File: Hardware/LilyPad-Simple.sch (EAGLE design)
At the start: 43 parts, among them U1 ATMEGA328P_TQFP, U2 MCP73831, U3 MIC5219 3.3V, Y1 8MHZ

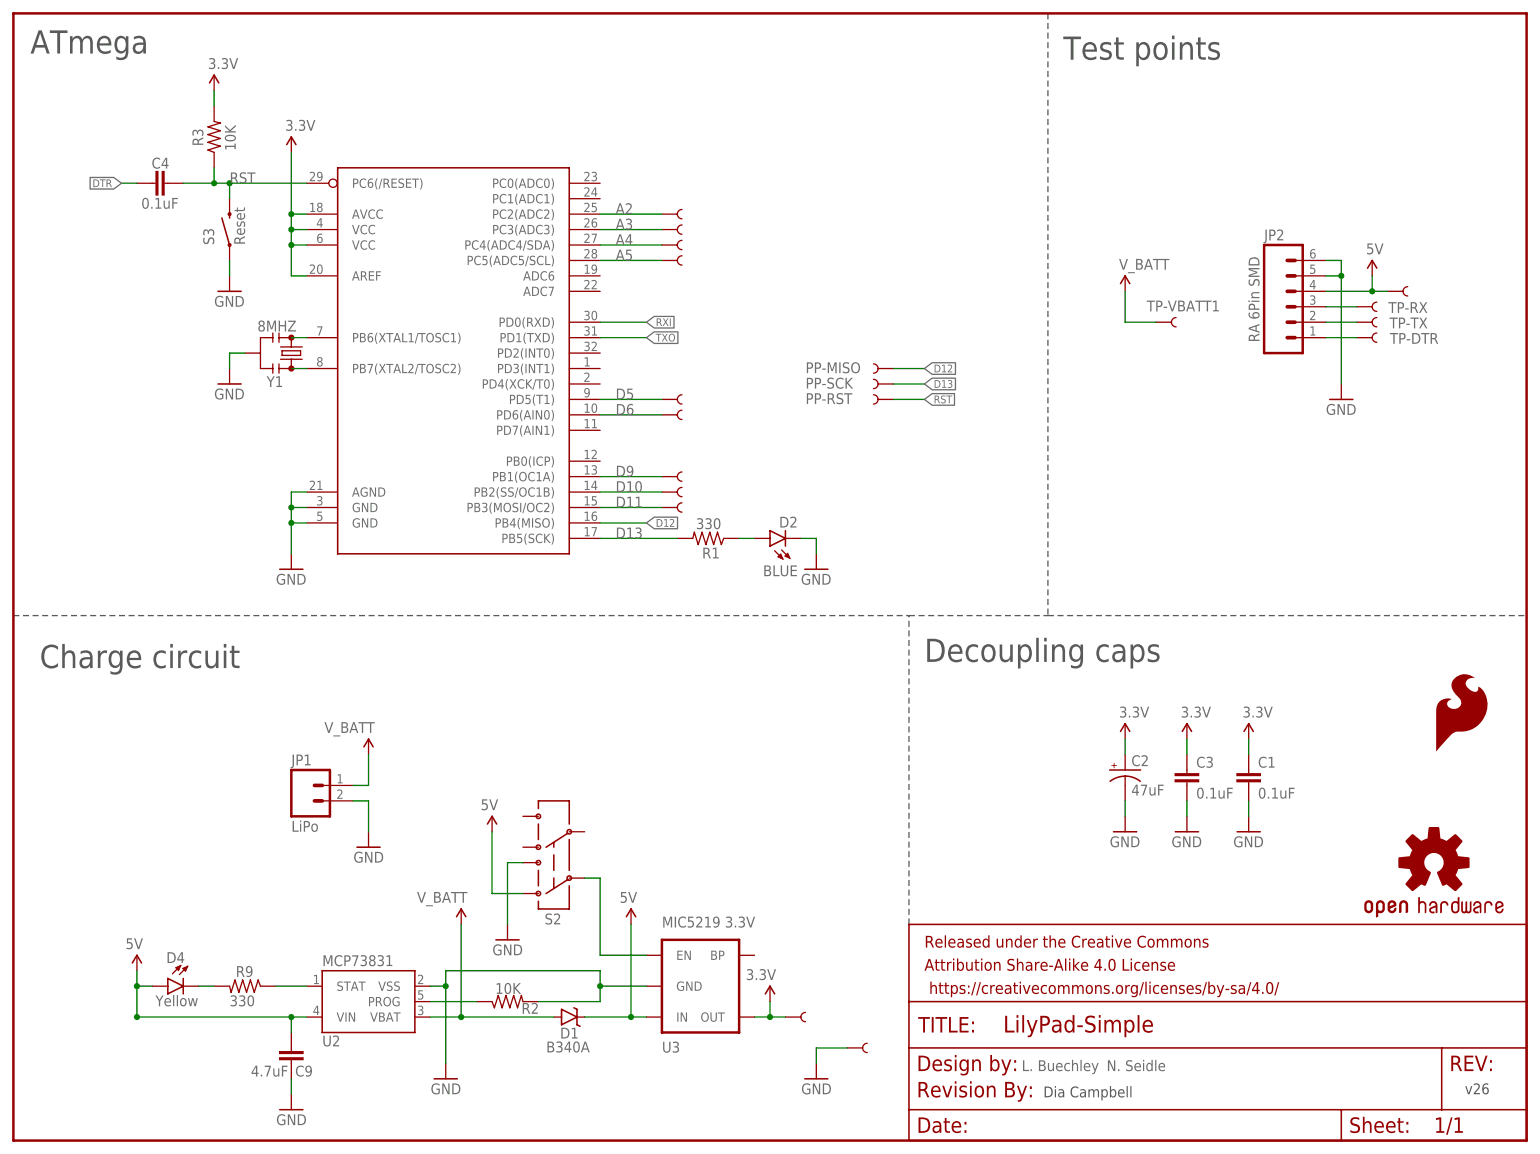
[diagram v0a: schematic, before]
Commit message: DRC changes, fixed some errors
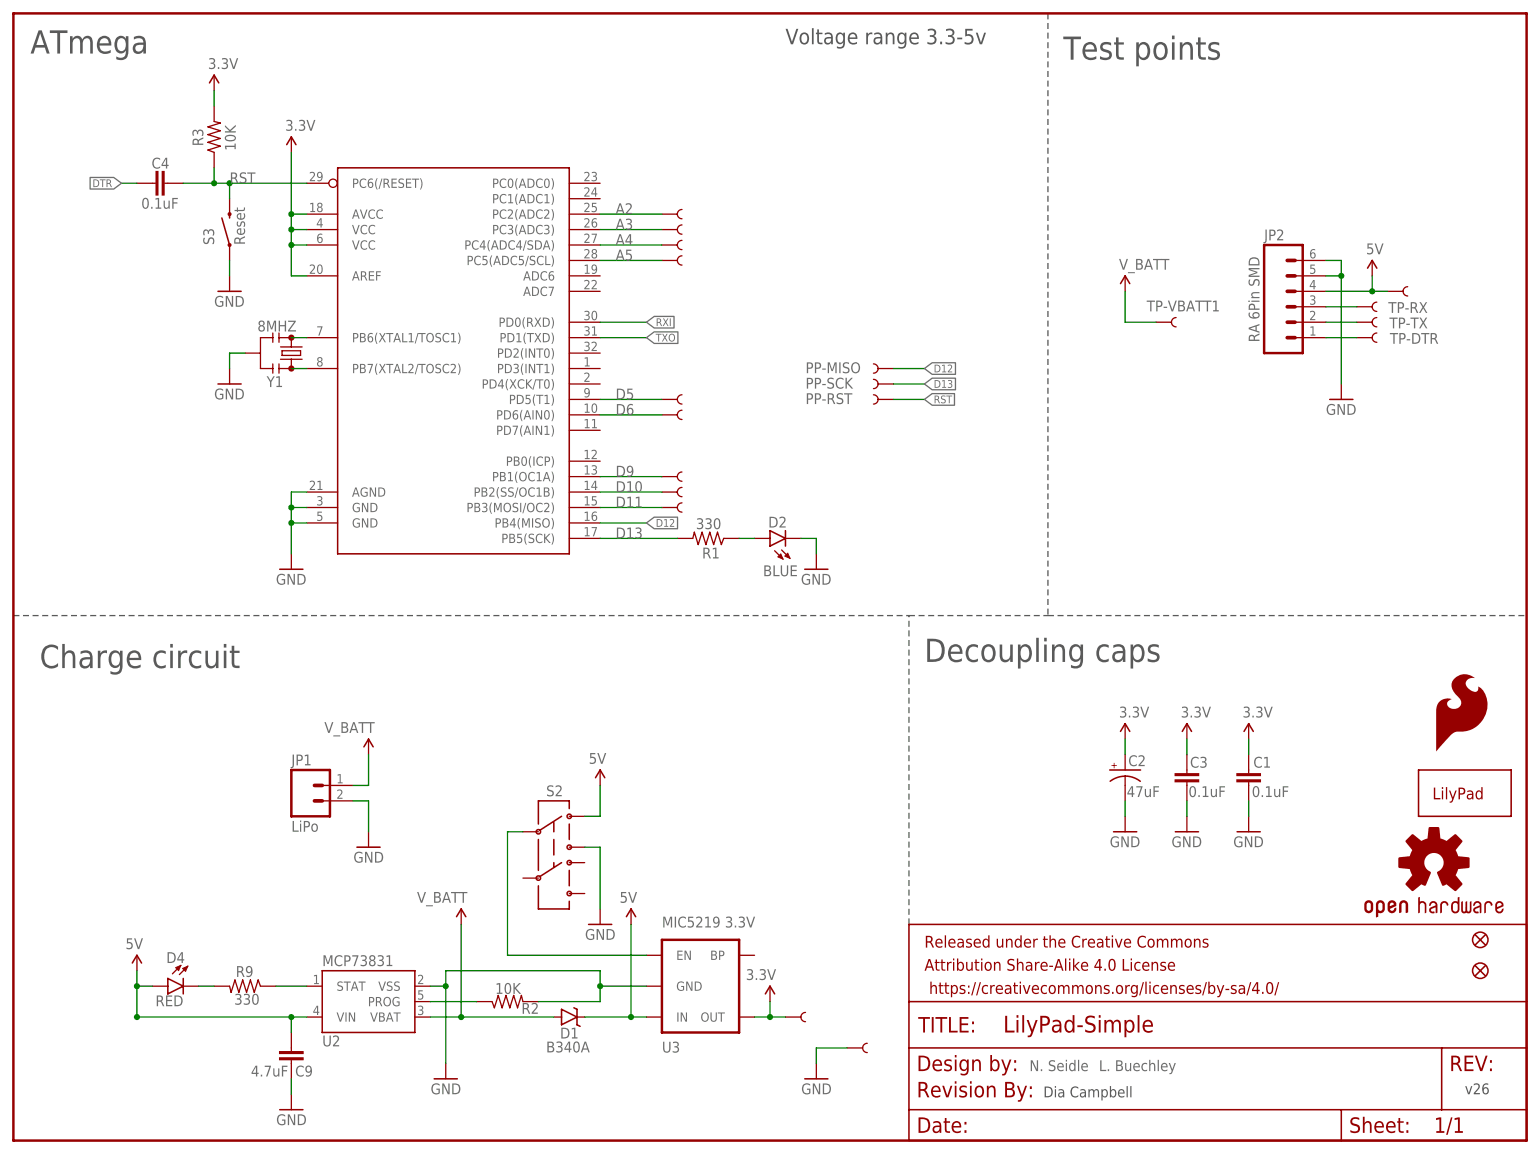
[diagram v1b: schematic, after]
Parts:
- added FID1, FID2: FIDUCIAL1X2, SparkFun-Aesthetics:FIDUCIAL1X2
- added U$2: LOGO-LPLPA, LilyPad-Wearables:LOGO-LPLPA
- D4: value Yellow -> RED; device SparkFun-LED:LED-YELLOW0603 -> SparkFun-LED:LED-RED0603
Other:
- note added: "Voltage range 3.3-5v"
- moved on the sheet: S2
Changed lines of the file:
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@@
 <part name="C9" library="SparkFun-Capacitors" deviceset="4.7UF-6.3V-10%(0603)" device="0603" value="4.7uF"/>
 <part name="GND18" library="supply1" deviceset="GND" device=""/>
-<part name="D4" library="SparkFun-LED" deviceset="LED-YELLOW" device="0603" value="Yellow"/>
+<part name="D4" library="SparkFun-LED" deviceset="LED-RED" device="0603" value="RED"/>
 <part name="R9" library="SparkFun-Resistors" deviceset="330OHM1/10W1%(0603)" device="" value="330"/>
 <part name="U2" library="SparkFun-PowerIC" deviceset="MCP73831" device=""/>
@@
 <part name="TP-VBATT1" library="SparkFun" deviceset="TEST-POINT" device="3X5" value=""/>
 <part name="SUPPLY8" library="SparkFun-Aesthetics" deviceset="V_BATT" device=""/>
+<part name="U$2" library="LilyPad-Wearables" deviceset="LOGO-LP" device="LPA"/>
+<part name="FID1" library="SparkFun-Aesthetics" deviceset="FIDUCIAL" device="1X2"/>
+<part name="FID2" library="SparkFun-Aesthetics" deviceset="FIDUCIAL" device="1X2"/>
 </parts>
 <sheets>
 <sheet>
 <plain>
-<text x="165.862" y="11.43" size="1.778" layer="95">L. Buechley</text>
-<text x="179.832" y="11.43" size="1.778" layer="95">N. Seidle</text>
+<text x="178.562" y="11.43" size="1.778" layer="95">L. Buechley</text>
+<text x="167.132" y="11.43" size="1.778" layer="95">N. Seidle</text>
 <text x="169.418" y="7.112" size="1.778" layer="97">Dia Campbell</text>
 <text x="238.76" y="7.62" size="1.778" layer="97">v26</text>
@@
 <text x="172.72" y="177.8" size="3.81" layer="97">Test points</text>
 <text x="2.794" y="178.816" size="3.81" layer="97">ATmega</text>
+<text x="127" y="180.34" size="2.54" layer="97">Voltage range 3.3-5v</text>
 </plain>
 <instances>
@@
 <instance part="A4/18" gate="G$1" x="109.22" y="147.32" smashed="yes"/>
 <instance part="D2" gate="G$1" x="124.46" y="99.06" smashed="yes" rot="R90">
-<attribute name="NAME" x="129.032" y="102.616" size="1.778" layer="95" rot="R180"/>
+<attribute name="NAME" x="127.254" y="102.616" size="1.778" layer="95" rot="R180"/>
 <attribute name="VALUE" x="129.032" y="94.615" size="1.778" layer="96" rot="R180"/>
 </instance>
@@
 <attribute name="VALUE" x="44.704" y="166.116" size="1.778" layer="96"/>
 </instance>
-<instance part="C1" gate="G$1" x="203.2" y="58.42"/>
+<instance part="C1" gate="G$1" x="203.2" y="58.42" smashed="yes">
+<attribute name="NAME" x="203.962" y="61.341" size="1.778" layer="95"/>
+<attribute name="VALUE" x="203.708" y="56.515" size="1.778" layer="96"/>
+</instance>
 <instance part="GND7" gate="1" x="203.2" y="50.8"/>
 <instance part="A5/19" gate="G$1" x="109.22" y="144.78" smashed="yes"/>
 <instance part="GND8" gate="1" x="132.08" y="10.16" rot="MR0"/>
 <instance part="U$4" gate="G$1" x="109.22" y="104.14" smashed="yes"/>
-<instance part="C2" gate="G$1" x="182.88" y="60.96"/>
-<instance part="C3" gate="G$1" x="193.04" y="58.42"/>
+<instance part="C2" gate="G$1" x="182.88" y="60.96" smashed="yes">
+<attribute name="NAME" x="183.388" y="61.595" size="1.778" layer="95"/>
+<attribute name="VALUE" x="183.134" y="56.515" size="1.778" layer="96"/>
+</instance>
+<instance part="C3" gate="G$1" x="193.04" y="58.42" smashed="yes">
+<attribute name="NAME" x="193.548" y="61.341" size="1.778" layer="95"/>
+<attribute name="VALUE" x="193.294" y="56.515" size="1.778" layer="96"/>
+</instance>
 <instance part="P+4" gate="G$1" x="203.2" y="66.04" smashed="yes">
 <attribute name="VALUE" x="202.184" y="69.596" size="1.778" layer="96"/>
@@
 </instance>
 <instance part="JP1" gate="G$1" x="48.26" y="55.88"/>
-<instance part="S2" gate="G$1" x="88.9" y="45.72" smashed="yes" rot="R180">
-<attribute name="NAME" x="87.376" y="37.338" size="1.778" layer="95" rot="MR180"/>
+<instance part="S2" gate="G$1" x="88.9" y="48.26" smashed="yes">
+<attribute name="NAME" x="90.424" y="56.642" size="1.778" layer="95" rot="MR0"/>
 </instance>
 <instance part="TP-TX" gate="G$1" x="220.98" y="134.62" smashed="yes">
@@
 <instance part="R9" gate="G$1" x="38.1" y="25.4" smashed="yes" rot="MR0">
 <attribute name="NAME" x="36.576" y="28.702" size="1.778" layer="95" rot="MR180"/>
-<attribute name="VALUE" x="35.56" y="23.876" size="1.778" layer="96" rot="MR180"/>
+<attribute name="VALUE" x="36.322" y="24.13" size="1.778" layer="96" rot="MR180"/>
 </instance>
 <instance part="U2" gate="G$1" x="58.42" y="22.86" rot="MR180"/>
@@
 <instance part="U3" gate="G$1" x="114.3" y="25.4" rot="MR180"/>
 <instance part="SUPPLY1" gate="G$1" x="223.52" y="142.24"/>
-<instance part="SUPPLY2" gate="G$1" x="78.74" y="50.8" rot="MR0"/>
-<instance part="GND10" gate="1" x="81.28" y="33.02" rot="MR0"/>
+<instance part="SUPPLY2" gate="G$1" x="96.52" y="58.42" rot="MR0"/>
+<instance part="GND10" gate="1" x="96.52" y="35.56" rot="MR0"/>
 <instance part="SUPPLY3" gate="G$1" x="73.66" y="35.56" rot="MR0"/>
 <instance part="SUPPLY4" gate="G$1" x="58.42" y="63.5" rot="MR0"/>
@@
 </instance>
 <instance part="SUPPLY8" gate="G$1" x="182.88" y="139.7"/>
+<instance part="U$2" gate="G$1" x="233.68" y="55.88"/>
+<instance part="FID1" gate="G$1" x="241.3" y="33.02"/>
+<instance part="FID2" gate="G$1" x="241.3" y="27.94"/>
 </instances>
 <busses>
@@
 <pinref part="S2" gate="G$1" pin="3"/>
 <pinref part="GND10" gate="1" pin="GND"/>
-<wire x1="83.82" y1="45.72" x2="81.28" y2="45.72" width="0.1524" layer="91"/>
-<wire x1="81.28" y1="45.72" x2="81.28" y2="35.56" width="0.1524" layer="91"/>
+<wire x1="93.98" y1="48.26" x2="96.52" y2="48.26" width="0.1524" layer="91"/>
+<wire x1="96.52" y1="48.26" x2="96.52" y2="38.1" width="0.1524" layer="91"/>
 </segment>
 <segment>
@@
 <segment>
 <pinref part="U3" gate="G$1" pin="EN"/>
-<wire x1="104.14" y1="30.48" x2="96.52" y2="30.48" width="0.1524" layer="91"/>
-<wire x1="96.52" y1="30.48" x2="96.52" y2="43.18" width="0.1524" layer="91"/>
+<wire x1="104.14" y1="30.48" x2="81.28" y2="30.48" width="0.1524" layer="91"/>
 <pinref part="S2" gate="G$1" pin="2"/>
-<wire x1="96.52" y1="43.18" x2="93.98" y2="43.18" width="0.1524" layer="91"/>
+<wire x1="81.28" y1="30.48" x2="81.28" y2="50.8" width="0.1524" layer="91"/>
+<wire x1="81.28" y1="50.8" x2="83.82" y2="50.8" width="0.1524" layer="91"/>
 </segment>
 </net>
@@
 <pinref part="S2" gate="G$1" pin="1"/>
 <pinref part="SUPPLY2" gate="G$1" pin="5V"/>
-<wire x1="83.82" y1="40.64" x2="78.74" y2="40.64" width="0.1524" layer="91"/>
-<wire x1="78.74" y1="40.64" x2="78.74" y2="50.8" width="0.1524" layer="91"/>
-</segment>
-<segment>
+<wire x1="93.98" y1="53.34" x2="96.52" y2="53.34" width="0.1524" layer="91"/>
+<wire x1="96.52" y1="53.34" x2="96.52" y2="58.42" width="0.1524" layer="91"/>
+</segment>
+<segment>

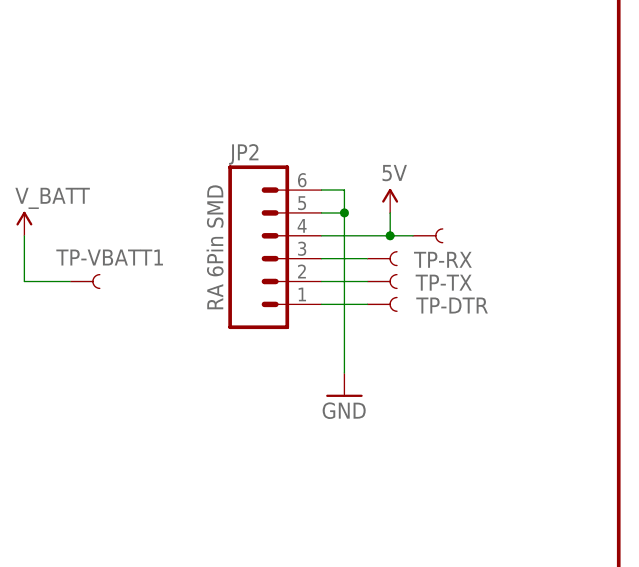
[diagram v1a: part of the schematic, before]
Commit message: Change to 3.3v connections
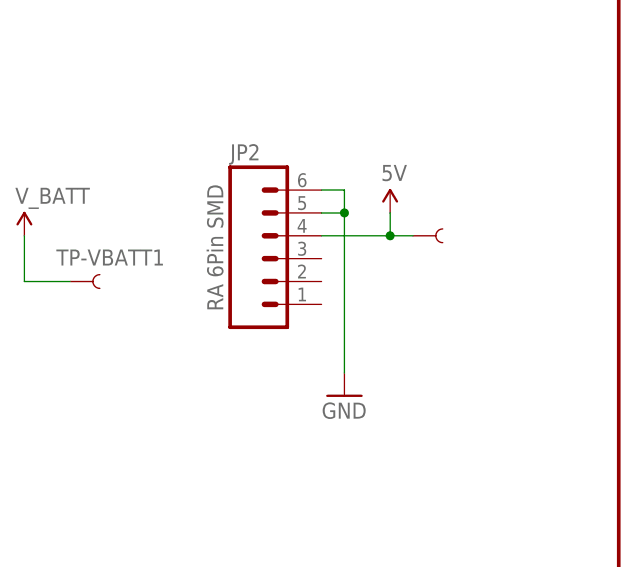
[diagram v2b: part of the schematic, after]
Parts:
- removed TP-DTR, TP-RX, TP-TX: TEST-POINT3X5, SparkFun:TEST-POINT3X5
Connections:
- removed net VCC: C1.1, C2.+, C3.1, R3.2, U1.AREF, U1.AVCC, U1.VCC@4, U1.VCC@6
- net 3.3V: now also C1.1, C2.+, C3.1, R3.2, U1.AREF, U1.AVCC, U1.VCC@4, U1.VCC@6
- net DTR: no longer JP2.1, TP-DTR.1
- net RXI: no longer JP2.3, TP-RX.1
- net TXO: no longer JP2.2, TP-TX.1
